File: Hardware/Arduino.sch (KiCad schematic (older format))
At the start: 17 parts, among them IC1 ATMEGA8-P, P1 CONN_5X2, P2 CONN_10, P3 CONN_10, P4 CONN_10, P5 CONN_10, SW1 SPST, X1 CRYSTAL

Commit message: added new files
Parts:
- added JP1: JUMPER, ~, symbol JUMPER
- added P6: CONN_7, symbol CONN_7
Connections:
- net 10: now also P4.10 (P10); no longer P4.9 (P9)
- net 11: now also P4.9 (P9); no longer P4.8 (P8)
- net 12: now also P4.8 (P8); no longer P4.7 (P7)
- net 13: now also P4.7 (P7); no longer P4.6 (P6)
- net 8: now also P5.2 (P2); no longer P5.1 (P1)
- net 9: now also P5.1 (P1); no longer P4.10 (P10)
- net GND: now also P4.6 (P6), P6.1 (P1)
- net RESET: now also JP1.1
- net RX: now also P6.4 (P4)
- net TX: now also P6.5 (P5)
- net VCC: now also P6.3 (P3)
- new net: JP1.2, P6.7 (P7)
- no-connect marks 13 -> 14
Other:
- note added: "7 PIN CONNECTOR\nDTR JUMPER"
- moved on the sheet: P1
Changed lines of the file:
@@
 Sheet 1 1
 Title ""
-Date "21 may 2015"
+Date "10 aug 2015"
 Rev ""
 Comp ""
@@
 Text Label 7800 2400 2    40   ~ 0
 AREF
-Text Label 7800 2500 2    40   ~ 0
+Text Label 7800 2600 2    40   ~ 0
 13
-Text Label 7800 2600 2    40   ~ 0
+Text Label 7800 2700 2    40   ~ 0
 12
-Text Label 7800 2700 2    40   ~ 0
+Text Label 7800 2800 2    40   ~ 0
 11
-Text Label 7800 2800 2    40   ~ 0
+Text Label 7800 2900 2    40   ~ 0
 10
-Text Label 7800 2900 2    40   ~ 0
+Text Label 7800 3150 2    40   ~ 0
 9
-Text Label 7800 3150 2    40   ~ 0
+Text Label 7800 3250 2    40   ~ 0
 8
 Text Label 7800 3850 2    40   ~ 0
@@
 NoConn ~ 6600 3450
 NoConn ~ 6600 3150
-NoConn ~ 7800 3250
 $Comp
 L CONN_10 P5
@@
 L CONN_5X2 P1
 U 1 1 55471021
-P 9850 1850
-F 0 "P1" H 9850 2150 60  0000 C CNN
-F 1 "CONN_5X2" V 9850 1850 50  0000 C CNN
-F 2 "" H 9850 1850 60  0000 C CNN
-F 3 "" H 9850 1850 60  0000 C CNN
-	1    9850 1850
-	1    0    0    -1
-$EndComp
-Text Label 9450 1650 2    60   ~ 0
+P 9950 1100
+F 0 "P1" H 9950 1400 60  0000 C CNN
+F 1 "CONN_5X2" V 9950 1100 50  0000 C CNN
+F 2 "" H 9950 1100 60  0000 C CNN
+F 3 "" H 9950 1100 60  0000 C CNN
+	1    9950 1100
+	1    0    0    -1
+$EndComp
+Text Label 9550 900  2    60   ~ 0
 MOSI
-Text Label 9450 1850 2    40   ~ 0
+Text Label 9550 1100 2    40   ~ 0
 RESET
-Text Label 9450 1950 2    60   ~ 0
+Text Label 9550 1200 2    60   ~ 0
 SCK
-Text Label 9450 2050 2    60   ~ 0
+Text Label 9550 1300 2    60   ~ 0
 MISO
-Text Label 10250 1650 0    60   ~ 0
+Text Label 10350 900  0    60   ~ 0
 VCC
 $Comp
 L GND #PWR09
 U 1 1 55471076
-P 10350 2150
-F 0 "#PWR09" H 10350 2150 30  0001 C CNN
-F 1 "GND" H 10350 2080 30  0001 C CNN
-F 2 "" H 10350 2150 60  0001 C CNN
-F 3 "" H 10350 2150 60  0001 C CNN
-	1    10350 2150
-	1    0    0    -1
-$EndComp
-Wire Wire Line
-	10250 1750 10350 1750
-Wire Wire Line
-	10350 1750 10350 2150
-Wire Wire Line
-	10250 1850 10350 1850
-Connection ~ 10350 1850
-Wire Wire Line
-	10250 1950 10350 1950
-Connection ~ 10350 1950
-Wire Wire Line
-	10250 2050 10350 2050
-Connection ~ 10350 2050
+P 10450 1400
+F 0 "#PWR09" H 10450 1400 30  0001 C CNN
+F 1 "GND" H 10450 1330 30  0001 C CNN
+F 2 "" H 10450 1400 60  0001 C CNN
+F 3 "" H 10450 1400 60  0001 C CNN
+	1    10450 1400
+	1    0    0    -1
+$EndComp
+Wire Wire Line
+	10350 1000 10450 1000
+Wire Wire Line
+	10450 1000 10450 1400
+Wire Wire Line
+	10350 1100 10450 1100
+Connection ~ 10450 1100
+Wire Wire Line
+	10350 1200 10450 1200
+Connection ~ 10450 1200
+Wire Wire Line
+	10350 1300 10450 1300
+Connection ~ 10450 1300
 Text Label 5200 2250 0    60   ~ 0
 MOSI
@@
 Wire Wire Line
 	5000 2450 5200 2450
-NoConn ~ 9450 1750
+NoConn ~ 9550 1000
 Wire Notes Line
 	500  5000 11200 5000
@@
 EndData
 $EndBitmap
+Text Notes 4100 150  0    60   ~ 0
+7 PIN CONNECTOR\nDTR JUMPER
+$Comp
+L CONN_7 P6
+U 1 1 55C82B83
+P 10350 2050
+F 0 "P6" V 10320 2050 60  0000 C CNN
+F 1 "CONN_7" V 10420 2050 60  0000 C CNN
+F 2 "" H 10350 2050 60  0000 C CNN
+F 3 "" H 10350 2050 60  0000 C CNN
+	1    10350 2050
+	1    0    0    -1
+$EndComp
+$Comp
+L GND #PWR010
+U 1 1 55C82B9B
+P 9250 1850
+F 0 "#PWR010" H 9250 1850 30  0001 C CNN
+F 1 "GND" H 9250 1780 30  0001 C CNN
+F 2 "" H 9250 1850 60  0001 C CNN
+F 3 "" H 9250 1850 60  0001 C CNN
+	1    9250 1850
+	1    0    0    -1
+$EndComp
+Wire Wire Line
+	10000 1750 9250 1750
+Wire Wire Line
+	9250 1750 9250 1850
+Text Label 10000 1950 2    60   ~ 0
+VCC
+Text Label 10000 2050 2    40   ~ 0
+RX
+Text Label 10000 2150 2    40   ~ 0
+TX
+NoConn ~ 10000 1850
+NoConn ~ 10000 2250
+$Comp
+L JUMPER JP1
+U 1 1 55C82C64
+P 9600 2350
+F 0 "JP1" H 9600 2500 60  0000 C CNN
+F 1 "JUMPER" H 9600 2270 40  0000 C CNN
+F 2 "~" H 9600 2350 60  0000 C CNN
+F 3 "~" H 9600 2350 60  0000 C CNN
+	1    9600 2350
+	1    0    0    -1
+$EndComp
+Wire Wire Line
+	9900 2350 10000 2350
+Text Label 9300 2350 2    40   ~ 0
+RESET
+$Comp
+L GND #PWR?
+U 1 1 55C86966
+P 7500 2550
+F 0 "#PWR?" H 7500 2550 30  0001 C CNN
+F 1 "GND" H 7500 2480 30  0001 C CNN
+F 2 "" H 7500 2550 60  0001 C CNN
+F 3 "" H 7500 2550 60  0001 C CNN
+	1    7500 2550
+	1    0    0    -1
+$EndComp
+Wire Wire Line
+	7500 2550 7500 2500
+Wire Wire Line
+	7500 2500 7800 2500
 $EndSCHEMATC

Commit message: added corrected files
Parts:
- added D4: LED, symbol LED
- added R4, R5: 1k, symbol R
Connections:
- net 13: now also D4.1 (A)
- net GND: now also R4.2, R5.2
- net at D2.2 (K), R3.1: no longer D3.2 (K)
- new net: D3.2 (K), R4.1
- new net: D4.2 (K), R5.1
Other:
- moved on the sheet: R3
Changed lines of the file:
@@
 LIBS:valves
 LIBS:Arduino-cache
-EELAYER 27 0
+EELAYER 25 0
 EELAYER END
 $Descr A4 11693 8268
@@
 VCC
 $Comp
-L GND #PWR01
+L GND #PWR3
 U 1 1 55092BF2
 P 2950 2450
-F 0 "#PWR01" H 2950 2450 30  0001 C CNN
+F 0 "#PWR3" H 2950 2450 30  0001 C CNN
 F 1 "GND" H 2950 2380 30  0001 C CNN
 F 2 "" H 2950 2450 60  0001 C CNN
@@
 VCC
 $Comp
-L GND #PWR02
+L GND #PWR9
 U 1 1 55092C1A
 P 9400 4000
-F 0 "#PWR02" H 9400 4000 30  0001 C CNN
+F 0 "#PWR9" H 9400 4000 30  0001 C CNN
 F 1 "GND" H 9400 3930 30  0001 C CNN
 F 2 "" H 9400 4000 60  0001 C CNN
@@
 VCC
 $Comp
-L GND #PWR03
+L GND #PWR4
 U 1 1 55092C40
 P 3850 1150
-F 0 "#PWR03" H 3850 1150 30  0001 C CNN
+F 0 "#PWR4" H 3850 1150 30  0001 C CNN
 F 1 "GND" H 3850 1080 30  0001 C CNN
 F 2 "" H 3850 1150 60  0001 C CNN
@@
 $EndComp
 $Comp
-L GND #PWR04
+L GND #PWR5
 U 1 1 55092C58
 P 4000 4700
-F 0 "#PWR04" H 4000 4700 30  0001 C CNN
+F 0 "#PWR5" H 4000 4700 30  0001 C CNN
 F 1 "GND" H 4000 4630 30  0001 C CNN
 F 2 "" H 4000 4700 60  0001 C CNN
@@
 $EndComp
 $Comp
-L GND #PWR05
+L GND #PWR1
 U 1 1 55092C5E
 P 1600 2800
-F 0 "#PWR05" H 1600 2800 30  0001 C CNN
+F 0 "#PWR1" H 1600 2800 30  0001 C CNN
 F 1 "GND" H 1600 2730 30  0001 C CNN
 F 2 "" H 1600 2800 60  0001 C CNN
@@
 $EndComp
 $Comp
-L GND #PWR06
+L GND #PWR2
 U 1 1 55092CB1
 P 2200 2350
-F 0 "#PWR06" H 2200 2350 30  0001 C CNN
+F 0 "#PWR2" H 2200 2350 30  0001 C CNN
 F 1 "GND" H 2200 2280 30  0001 C CNN
 F 2 "" H 2200 2350 60  0001 C CNN
@@
 VCC
 $Comp
-L GND #PWR07
+L GND #PWR6
 U 1 1 5509301E
 P 7500 2150
-F 0 "#PWR07" H 7500 2150 30  0001 C CNN
+F 0 "#PWR6" H 7500 2150 30  0001 C CNN
 F 1 "GND" H 7500 2080 30  0001 C CNN
 F 2 "" H 7500 2150 60  0001 C CNN
@@
 L R R3
 U 1 1 55431020
-P 10100 3700
-F 0 "R3" V 10180 3700 50  0000 C CNN
-F 1 "1k" V 10100 3700 50  0000 C CNN
-F 2 "" H 10100 3700 60  0001 C CNN
-F 3 "" H 10100 3700 60  0001 C CNN
-	1    10100 3700
-	1    0    0    -1
-$EndComp
-Wire Wire Line
-	9950 3400 10300 3400
-Wire Wire Line
-	10100 3400 10100 3450
-Connection ~ 10100 3400
-$Comp
-L GND #PWR08
+P 9950 3700
+F 0 "R3" V 10030 3700 50  0000 C CNN
+F 1 "1k" V 9950 3700 50  0000 C CNN
+F 2 "" H 9950 3700 60  0001 C CNN
+F 3 "" H 9950 3700 60  0001 C CNN
+	1    9950 3700
+	1    0    0    -1
+$EndComp
+$Comp
+L GND #PWR10
 U 1 1 5543108C
-P 10100 4000
-F 0 "#PWR08" H 10100 4000 30  0001 C CNN
-F 1 "GND" H 10100 3930 30  0001 C CNN
-F 2 "" H 10100 4000 60  0001 C CNN
-F 3 "" H 10100 4000 60  0001 C CNN
-	1    10100 4000
-	1    0    0    -1
-$EndComp
-Wire Wire Line
-	10100 3950 10100 4000
+P 9950 4000
+F 0 "#PWR10" H 9950 4000 30  0001 C CNN
+F 1 "GND" H 9950 3930 30  0001 C CNN
+F 2 "" H 9950 4000 60  0001 C CNN
+F 3 "" H 9950 4000 60  0001 C CNN
+	1    9950 4000
+	1    0    0    -1
+$EndComp
 Text Label 9950 3000 0    40   ~ 0
 RX
@@
 VCC
 $Comp
-L GND #PWR09
+L GND #PWR11
 U 1 1 55471076
 P 10450 1400
-F 0 "#PWR09" H 10450 1400 30  0001 C CNN
+F 0 "#PWR11" H 10450 1400 30  0001 C CNN
 F 1 "GND" H 10450 1330 30  0001 C CNN
 F 2 "" H 10450 1400 60  0001 C CNN
@@
 43 7C 02 00 00 84 0C F1 09 00 00 10 32 C4 27 00 00 40 C8 10 9F 00 00 00 21 43 7C 02 00 00 84 0C
 F1 09 00 00 10 32 C4 27 00 00 40 C8 10 9F 00 00 00 21 43 7C 02 00 00 84 EC FF 02 24 05 F2 19 03
-C8 1D 6B 00 00 00 00 49 45 4E 44 AE 42 60 82 00 $EndBitmap
+C8 1D 6B 00 00 00 00 49 45 4E 44 AE 42 60 82 00
 EndData
 $EndBitmap
@@
 $EndComp
 $Comp
-L GND #PWR010
+L GND #PWR8
 U 1 1 55C82B9B
 P 9250 1850
-F 0 "#PWR010" H 9250 1850 30  0001 C CNN
+F 0 "#PWR8" H 9250 1850 30  0001 C CNN
 F 1 "GND" H 9250 1780 30  0001 C CNN
 F 2 "" H 9250 1850 60  0001 C CNN
@@
 RESET
 $Comp
-L GND #PWR?
+L GND #PWR7
 U 1 1 55C86966
 P 7500 2550
-F 0 "#PWR?" H 7500 2550 30  0001 C CNN
+F 0 "#PWR7" H 7500 2550 30  0001 C CNN
 F 1 "GND" H 7500 2480 30  0001 C CNN
 F 2 "" H 7500 2550 60  0001 C CNN
@@
 Wire Wire Line
 	7500 2500 7800 2500
+Wire Wire Line
+	9950 3400 9950 3450
+Wire Wire Line
+	9950 3950 9950 4000
+$Comp
+L R R4
+U 1 1 55D2ADA3
+P 10300 3700
+F 0 "R4" V 10380 3700 50  0000 C CNN
+F 1 "1k" V 10300 3700 50  0000 C CNN
+F 2 "" H 10300 3700 60  0001 C CNN
+F 3 "" H 10300 3700 60  0001 C CNN
+	1    10300 3700
+	1    0    0    -1
+$EndComp
+Wire Wire Line
+	10300 3400 10300 3450
+Wire Wire Line
+	9950 3950 10750 3950
+$Comp
+L LED D4
+U 1 1 55D2B050
+P 10750 3200
+F 0 "D4" H 10750 3300 50  0000 C CNN
+F 1 "LED" H 10750 3100 50  0000 C CNN
+F 2 "" H 10750 3200 60  0001 C CNN
+F 3 "" H 10750 3200 60  0001 C CNN
+	1    10750 3200
+	0    1    1    0
+$EndComp
+$Comp
+L R R5
+U 1 1 55D2B08B
+P 10750 3700
+F 0 "R5" V 10830 3700 50  0000 C CNN
+F 1 "1k" V 10750 3700 50  0000 C CNN
+F 2 "" H 10750 3700 60  0001 C CNN
+F 3 "" H 10750 3700 60  0001 C CNN
+	1    10750 3700
+	1    0    0    -1
+$EndComp
+Connection ~ 10300 3950
+Wire Wire Line
+	10750 3400 10750 3450
+Text Label 10750 3000 2    40   ~ 0
+13
 $EndSCHEMATC

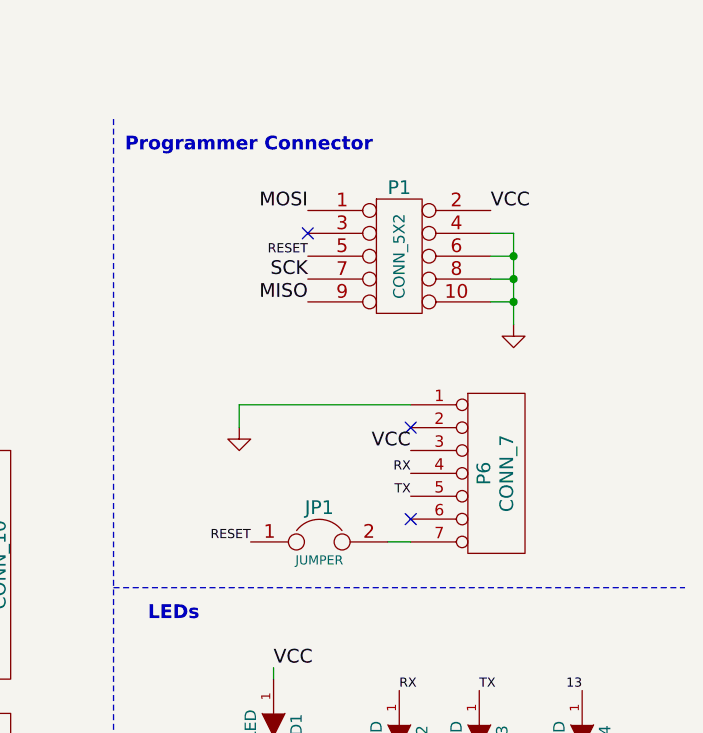
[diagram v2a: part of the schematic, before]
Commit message: added capacitor
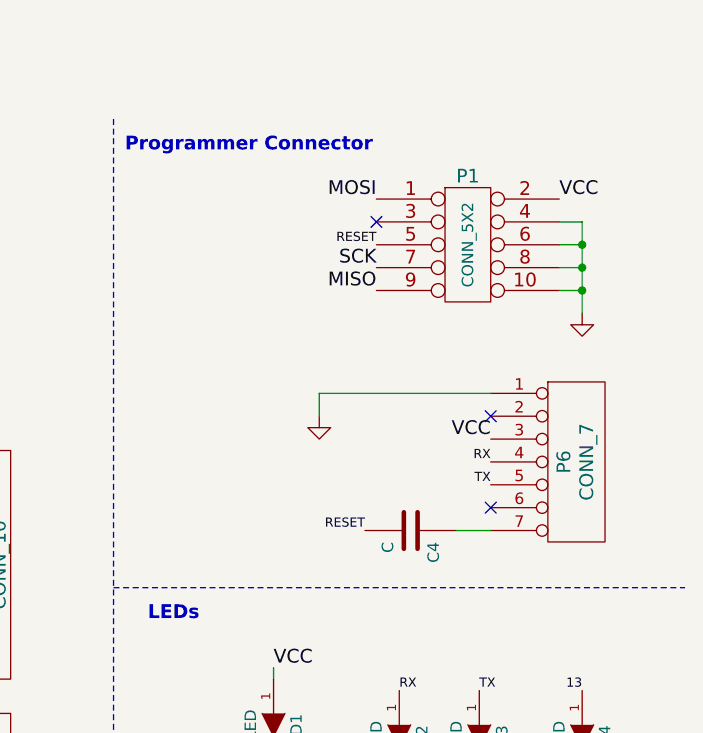
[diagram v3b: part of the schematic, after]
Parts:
- removed JP1: JUMPER, ~, symbol JUMPER
- added C4: C, symbol C
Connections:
- net RESET: now also C4.2
- net at P6.7 (P7): now also C4.1
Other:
- moved on the sheet: P1, P6
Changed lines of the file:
@@
 VCC
 $Comp
-L GND #PWR9
+L GND #PWR8
 U 1 1 55092C1A
 P 9400 4000
-F 0 "#PWR9" H 9400 4000 30  0001 C CNN
+F 0 "#PWR8" H 9400 4000 30  0001 C CNN
 F 1 "GND" H 9400 3930 30  0001 C CNN
 F 2 "" H 9400 4000 60  0001 C CNN
@@
 L CONN_5X2 P1
 U 1 1 55471021
-P 9950 1100
-F 0 "P1" H 9950 1400 60  0000 C CNN
-F 1 "CONN_5X2" V 9950 1100 50  0000 C CNN
-F 2 "" H 9950 1100 60  0000 C CNN
-F 3 "" H 9950 1100 60  0000 C CNN
-	1    9950 1100
-	1    0    0    -1
-$EndComp
-Text Label 9550 900  2    60   ~ 0
+P 10250 1050
+F 0 "P1" H 10250 1350 60  0000 C CNN
+F 1 "CONN_5X2" V 10250 1050 50  0000 C CNN
+F 2 "" H 10250 1050 60  0000 C CNN
+F 3 "" H 10250 1050 60  0000 C CNN
+	1    10250 1050
+	1    0    0    -1
+$EndComp
+Text Label 9850 850  2    60   ~ 0
 MOSI
-Text Label 9550 1100 2    40   ~ 0
+Text Label 9850 1050 2    40   ~ 0
 RESET
-Text Label 9550 1200 2    60   ~ 0
+Text Label 9850 1150 2    60   ~ 0
 SCK
-Text Label 9550 1300 2    60   ~ 0
+Text Label 9850 1250 2    60   ~ 0
 MISO
-Text Label 10350 900  0    60   ~ 0
+Text Label 10650 850  0    60   ~ 0
 VCC
 $Comp
 L GND #PWR11
 U 1 1 55471076
-P 10450 1400
-F 0 "#PWR11" H 10450 1400 30  0001 C CNN
-F 1 "GND" H 10450 1330 30  0001 C CNN
-F 2 "" H 10450 1400 60  0001 C CNN
-F 3 "" H 10450 1400 60  0001 C CNN
-	1    10450 1400
-	1    0    0    -1
-$EndComp
-Wire Wire Line
-	10350 1000 10450 1000
-Wire Wire Line
-	10450 1000 10450 1400
-Wire Wire Line
-	10350 1100 10450 1100
-Connection ~ 10450 1100
-Wire Wire Line
-	10350 1200 10450 1200
-Connection ~ 10450 1200
-Wire Wire Line
-	10350 1300 10450 1300
-Connection ~ 10450 1300
+P 10750 1350
+F 0 "#PWR11" H 10750 1350 30  0001 C CNN
+F 1 "GND" H 10750 1280 30  0001 C CNN
+F 2 "" H 10750 1350 60  0001 C CNN
+F 3 "" H 10750 1350 60  0001 C CNN
+	1    10750 1350
+	1    0    0    -1
+$EndComp
+Wire Wire Line
+	10650 950  10750 950
+Wire Wire Line
+	10750 950  10750 1350
+Wire Wire Line
+	10650 1050 10750 1050
+Connection ~ 10750 1050
+Wire Wire Line
+	10650 1150 10750 1150
+Connection ~ 10750 1150
+Wire Wire Line
+	10650 1250 10750 1250
+Connection ~ 10750 1250
 Text Label 5200 2250 0    60   ~ 0
 MOSI
@@
 Wire Wire Line
 	5000 2450 5200 2450
-NoConn ~ 9550 1000
+NoConn ~ 9850 950
 Wire Notes Line
 	500  5000 11200 5000
@@
 L CONN_7 P6
 U 1 1 55C82B83
-P 10350 2050
-F 0 "P6" V 10320 2050 60  0000 C CNN
-F 1 "CONN_7" V 10420 2050 60  0000 C CNN
-F 2 "" H 10350 2050 60  0000 C CNN
-F 3 "" H 10350 2050 60  0000 C CNN
-	1    10350 2050
-	1    0    0    -1
-$EndComp
-$Comp
-L GND #PWR8
+P 10700 2000
+F 0 "P6" V 10670 2000 60  0000 C CNN
+F 1 "CONN_7" V 10770 2000 60  0000 C CNN
+F 2 "" H 10700 2000 60  0000 C CNN
+F 3 "" H 10700 2000 60  0000 C CNN
+	1    10700 2000
+	1    0    0    -1
+$EndComp
+$Comp
+L GND #PWR9
 U 1 1 55C82B9B
-P 9250 1850
-F 0 "#PWR8" H 9250 1850 30  0001 C CNN
-F 1 "GND" H 9250 1780 30  0001 C CNN
-F 2 "" H 9250 1850 60  0001 C CNN
-F 3 "" H 9250 1850 60  0001 C CNN
-	1    9250 1850
-	1    0    0    -1
-$EndComp
-Wire Wire Line
-	10000 1750 9250 1750
-Wire Wire Line
-	9250 1750 9250 1850
-Text Label 10000 1950 2    60   ~ 0
+P 9600 1800
+F 0 "#PWR9" H 9600 1800 30  0001 C CNN
+F 1 "GND" H 9600 1730 30  0001 C CNN
+F 2 "" H 9600 1800 60  0001 C CNN
+F 3 "" H 9600 1800 60  0001 C CNN
+	1    9600 1800
+	1    0    0    -1
+$EndComp
+Wire Wire Line
+	10350 1700 9600 1700
+Wire Wire Line
+	9600 1700 9600 1800
+Text Label 10350 1900 2    60   ~ 0
 VCC
-Text Label 10000 2050 2    40   ~ 0
+Text Label 10350 2000 2    40   ~ 0
 RX
-Text Label 10000 2150 2    40   ~ 0
+Text Label 10350 2100 2    40   ~ 0
 TX
-NoConn ~ 10000 1850
-NoConn ~ 10000 2250
-$Comp
-L JUMPER JP1
-U 1 1 55C82C64
-P 9600 2350
-F 0 "JP1" H 9600 2500 60  0000 C CNN
-F 1 "JUMPER" H 9600 2270 40  0000 C CNN
-F 2 "~" H 9600 2350 60  0000 C CNN
-F 3 "~" H 9600 2350 60  0000 C CNN
-	1    9600 2350
-	1    0    0    -1
-$EndComp
-Wire Wire Line
-	9900 2350 10000 2350
-Text Label 9300 2350 2    40   ~ 0
+NoConn ~ 10350 1800
+NoConn ~ 10350 2200
+Wire Wire Line
+	10200 2300 10350 2300
+Text Label 9800 2300 2    40   ~ 0
 RESET
 $Comp
@@
 Text Label 10750 3000 2    40   ~ 0
 13
+$Comp
+L C C4
+U 1 1 55EFADFD
+P 10000 2300
+F 0 "C4" H 10050 2400 50  0000 L CNN
+F 1 "C" H 10050 2200 50  0000 L CNN
+F 2 "" H 10038 2150 30  0000 C CNN
+F 3 "" H 10000 2300 60  0000 C CNN
+	1    10000 2300
+	0    1    1    0
+$EndComp
 $EndSCHEMATC
